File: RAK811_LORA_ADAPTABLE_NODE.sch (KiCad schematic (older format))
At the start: 18 parts, among them J1 Screw_Terminal_01x02, J2 Screw_Terminal_01x03, J3 Conn_01x01_Male, J4 Conn_01x01_Male, J5 Conn_01x01_Male, J6 Conn_01x01_Male, J7 Conn_Coaxial, U1 RAK811-HF

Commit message: some i/o pins layout
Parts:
- removed H1, H6: MountingHole, MountingHole:MountingHole_3mm, symbol Mechanical:MountingHole
- added J10, J11, J12, J13, J14, J15, J8, J9: Conn_01x01_Male, Connector_Wire:SolderWirePad_1x01_Drill0.8mm, symbol Connector:Conn_01x01_Male
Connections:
- net at BT2.2 (-), J7.2 (Ext), U1.1 (GND)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: now also J1.1 (Pin_1), J12.1 (Pin_1); no longer J1.2 (Pin_2)
- net at JP1.2 (C), U1.11 (VCC): now also J1.2 (Pin_2), J15.1 (Pin_1); no longer J1.1 (Pin_1)
- net at U1.13 (PA14): now also J8.1 (Pin_1)
- net at U1.14 (PA15): now also J10.1 (Pin_1)
- net at U1.15 (PB3): now also J13.1 (Pin_1)
- net at U1.16 (PB5): now also J9.1 (Pin_1)
- net at U1.2 (PB12): now also J14.1 (Pin_1)
- net at U1.27 (PB2/BOOT1): now also J11.1 (Pin_1)
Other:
- moved on the sheet: H2, H3, H4, H5
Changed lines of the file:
@@
 $EndDescr
-$Comp
-L Mechanical:MountingHole H1
-U 1 1 5EED2AEB
-P 4200 5600
-F 0 "H1" H 4300 5646 50  0000 L CNN
-F 1 "MountingHole" H 4300 5555 50  0000 L CNN
-F 2 "MountingHole:MountingHole_3mm" H 4200 5600 50  0001 C CNN
-F 3 "~" H 4200 5600 50  0001 C CNN
-	1    4200 5600
-	1    0    0    -1
-$EndComp
 $Comp
 L Mechanical:MountingHole H2
 U 1 1 5EED2E39
-P 4200 5800
-F 0 "H2" H 4300 5846 50  0000 L CNN
-F 1 "MountingHole" H 4300 5755 50  0000 L CNN
-F 2 "MountingHole:MountingHole_3mm" H 4200 5800 50  0001 C CNN
-F 3 "~" H 4200 5800 50  0001 C CNN
-	1    4200 5800
+P 3650 4600
+F 0 "H2" H 3750 4646 50  0000 L CNN
+F 1 "MountingHole" H 3750 4555 50  0000 L CNN
+F 2 "MountingHole:MountingHole_3mm" H 3650 4600 50  0001 C CNN
+F 3 "~" H 3650 4600 50  0001 C CNN
+	1    3650 4600
 	1    0    0    -1
 $EndComp
@@
 L Mechanical:MountingHole H3
 U 1 1 5EED3144
-P 4200 6000
-F 0 "H3" H 4300 6046 50  0000 L CNN
-F 1 "MountingHole" H 4300 5955 50  0000 L CNN
-F 2 "MountingHole:MountingHole_3mm" H 4200 6000 50  0001 C CNN
-F 3 "~" H 4200 6000 50  0001 C CNN
-	1    4200 6000
+P 3650 4800
+F 0 "H3" H 3750 4846 50  0000 L CNN
+F 1 "MountingHole" H 3750 4755 50  0000 L CNN
+F 2 "MountingHole:MountingHole_3mm" H 3650 4800 50  0001 C CNN
+F 3 "~" H 3650 4800 50  0001 C CNN
+	1    3650 4800
 	1    0    0    -1
 $EndComp
@@
 L Mechanical:MountingHole H4
 U 1 1 5EED33AC
-P 5050 5600
-F 0 "H4" H 5150 5646 50  0000 L CNN
-F 1 "MountingHole" H 5150 5555 50  0000 L CNN
-F 2 "MountingHole:MountingHole_3mm" H 5050 5600 50  0001 C CNN
-F 3 "~" H 5050 5600 50  0001 C CNN
-	1    5050 5600
-	1    0    0    -1
-$EndComp
-$Comp
-L Mechanical:MountingHole H6
-U 1 1 5EED36FB
-P 5050 6000
-F 0 "H6" H 5150 6046 50  0000 L CNN
-F 1 "MountingHole" H 5150 5955 50  0000 L CNN
-F 2 "MountingHole:MountingHole_3mm" H 5050 6000 50  0001 C CNN
-F 3 "~" H 5050 6000 50  0001 C CNN
-	1    5050 6000
+P 4500 4400
+F 0 "H4" H 4600 4446 50  0000 L CNN
+F 1 "MountingHole" H 4600 4355 50  0000 L CNN
+F 2 "MountingHole:MountingHole_3mm" H 4500 4400 50  0001 C CNN
+F 3 "~" H 4500 4400 50  0001 C CNN
+	1    4500 4400
 	1    0    0    -1
 $EndComp
@@
 L Mechanical:MountingHole H5
 U 1 1 5EED3A44
-P 5050 5800
-F 0 "H5" H 5150 5846 50  0000 L CNN
-F 1 "MountingHole" H 5150 5755 50  0000 L CNN
-F 2 "MountingHole:MountingHole_3mm" H 5050 5800 50  0001 C CNN
-F 3 "~" H 5050 5800 50  0001 C CNN
-	1    5050 5800
+P 4500 4600
+F 0 "H5" H 4600 4646 50  0000 L CNN
+F 1 "MountingHole" H 4600 4555 50  0000 L CNN
+F 2 "MountingHole:MountingHole_3mm" H 4500 4600 50  0001 C CNN
+F 3 "~" H 4500 4600 50  0001 C CNN
+	1    4500 4600
 	1    0    0    -1
 $EndComp
@@
 $EndComp
 Wire Wire Line
-	7550 1950 7550 1850
-Wire Wire Line
-	7550 1850 5450 1850
-Connection ~ 5450 1850
-Wire Wire Line
-	7550 2050 7000 2050
-Wire Wire Line
-	7000 2050 7000 4200
-Wire Wire Line
 	7000 4200 5850 4200
 Connection ~ 5850 4200
@@
 	7750 4200 7000 4200
 Connection ~ 7000 4200
+Wire Wire Line
+	7550 1950 7000 1950
+Wire Wire Line
+	7000 1950 7000 4200
+Wire Wire Line
+	7550 2050 7150 2050
+Wire Wire Line
+	7150 2050 7150 1850
+Wire Wire Line
+	7150 1850 5450 1850
+Connection ~ 5450 1850
+$Comp
+L Connector:Conn_01x01_Male J8
+U 1 1 5EF586B6
+P 4150 3150
+F 0 "J8" H 4258 3331 50  0000 C CNN
+F 1 "Conn_01x01_Male" H 4258 3240 50  0000 C CNN
+F 2 "Connector_Wire:SolderWirePad_1x01_Drill0.8mm" H 4150 3150 50  0001 C CNN
+F 3 "~" H 4150 3150 50  0001 C CNN
+	1    4150 3150
+	1    0    0    -1
+$EndComp
+Wire Wire Line
+	4350 3150 4550 3150
+$Comp
+L Connector:Conn_01x01_Male J9
+U 1 1 5EF61769
+P 6750 2650
+F 0 "J9" H 6722 2674 50  0000 R CNN
+F 1 "Conn_01x01_Male" H 6722 2583 50  0000 R CNN
+F 2 "Connector_Wire:SolderWirePad_1x01_Drill0.8mm" H 6750 2650 50  0001 C CNN
+F 3 "~" H 6750 2650 50  0001 C CNN
+	1    6750 2650
+	-1   0    0    -1
+$EndComp
+$Comp
+L Connector:Conn_01x01_Male J10
+U 1 1 5EF6CBB4
+P 4150 3250
+F 0 "J10" H 4258 3431 50  0000 C CNN
+F 1 "Conn_01x01_Male" H 4258 3340 50  0000 C CNN
+F 2 "Connector_Wire:SolderWirePad_1x01_Drill0.8mm" H 4150 3250 50  0001 C CNN
+F 3 "~" H 4150 3250 50  0001 C CNN
+	1    4150 3250
+	1    0    0    -1
+$EndComp
+Wire Wire Line
+	4350 3250 4550 3250
+$Comp
+L Connector:Conn_01x01_Male J11
+U 1 1 5EF78D3D
+P 6750 2350
+F 0 "J11" H 6722 2374 50  0000 R CNN
+F 1 "Conn_01x01_Male" H 6722 2283 50  0000 R CNN
+F 2 "Connector_Wire:SolderWirePad_1x01_Drill0.8mm" H 6750 2350 50  0001 C CNN
+F 3 "~" H 6750 2350 50  0001 C CNN
+	1    6750 2350
+	-1   0    0    -1
+$EndComp
+$Comp
+L Connector:Conn_01x01_Male J12
+U 1 1 5EF83DA7
+P 6150 4400
+F 0 "J12" H 6122 4424 50  0000 R CNN
+F 1 "Conn_01x01_Male" H 6122 4333 50  0000 R CNN
+F 2 "Connector_Wire:SolderWirePad_1x01_Drill0.8mm" H 6150 4400 50  0001 C CNN
+F 3 "~" H 6150 4400 50  0001 C CNN
+	1    6150 4400
+	-1   0    0    -1
+$EndComp
+Wire Wire Line
+	5950 4400 5850 4400
+Wire Wire Line
+	5850 4400 5850 4200
+$Comp
+L Connector:Conn_01x01_Male J13
+U 1 1 5EF91077
+P 6750 2450
+F 0 "J13" H 6722 2474 50  0000 R CNN
+F 1 "Conn_01x01_Male" H 6722 2383 50  0000 R CNN
+F 2 "Connector_Wire:SolderWirePad_1x01_Drill0.8mm" H 6750 2450 50  0001 C CNN
+F 3 "~" H 6750 2450 50  0001 C CNN
+	1    6750 2450
+	-1   0    0    -1
+$EndComp
+Wire Wire Line
+	6350 2450 6550 2450
+$Comp
+L Connector:Conn_01x01_Male J14
+U 1 1 5EF9D3AA
+P 6750 3150
+F 0 "J14" H 6722 3174 50  0000 R CNN
+F 1 "Conn_01x01_Male" H 6722 3083 50  0000 R CNN
+F 2 "Connector_Wire:SolderWirePad_1x01_Drill0.8mm" H 6750 3150 50  0001 C CNN
+F 3 "~" H 6750 3150 50  0001 C CNN
+	1    6750 3150
+	-1   0    0    -1
+$EndComp
+Wire Wire Line
+	6350 3150 6550 3150
+$Comp
+L Connector:Conn_01x01_Male J15
+U 1 1 5EFB7B96
+P 5750 1700
+F 0 "J15" H 5722 1724 50  0000 R CNN
+F 1 "Conn_01x01_Male" H 5722 1633 50  0000 R CNN
+F 2 "Connector_Wire:SolderWirePad_1x01_Drill0.8mm" H 5750 1700 50  0001 C CNN
+F 3 "~" H 5750 1700 50  0001 C CNN
+	1    5750 1700
+	-1   0    0    -1
+$EndComp
+Wire Wire Line
+	5550 1700 5450 1700
+Wire Wire Line
+	5450 1700 5450 1850
+Wire Wire Line
+	6350 2350 6550 2350
+Wire Wire Line
+	6350 2650 6550 2650
 $EndSCHEMATC

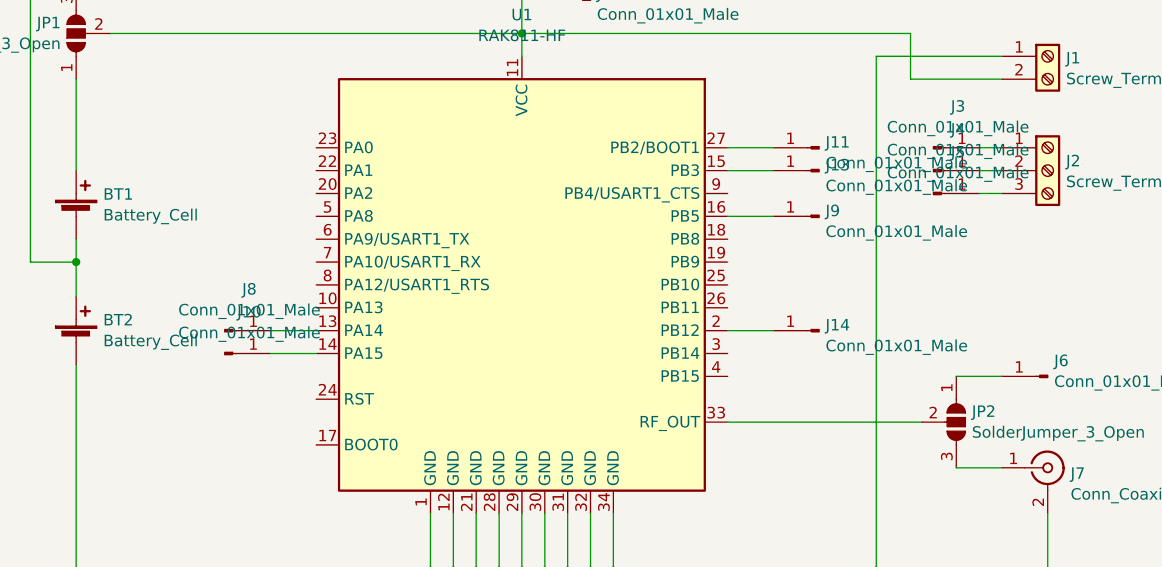
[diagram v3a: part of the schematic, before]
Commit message: half i/o pins layout
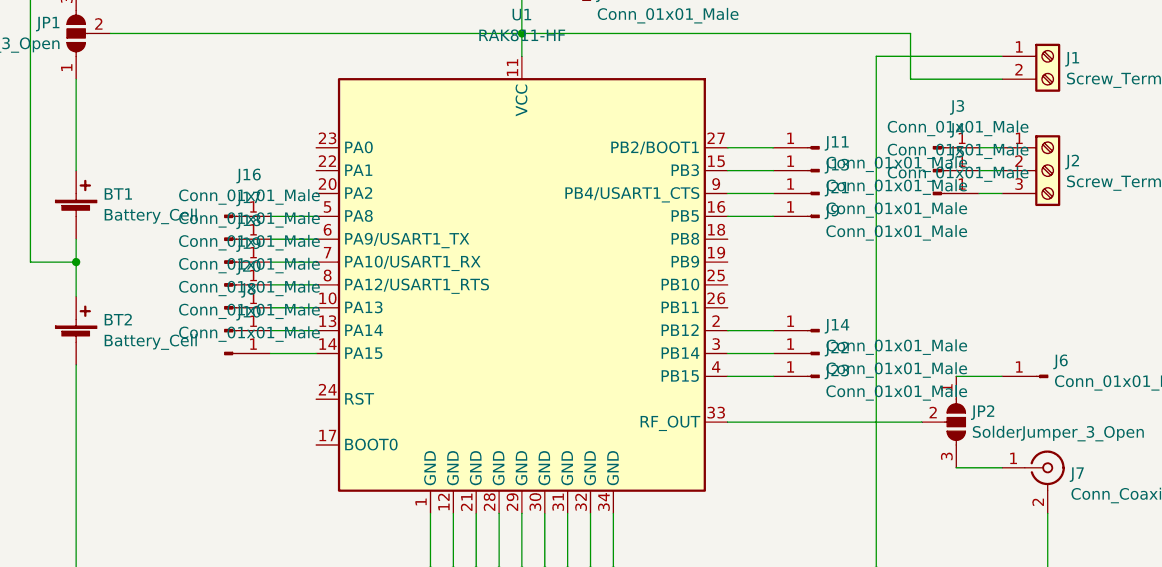
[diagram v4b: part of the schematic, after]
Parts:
- added J16, J17, J18, J19, J20, J21, J22, J23: Conn_01x01_Male, Connector_Wire:SolderWirePad_1x01_Drill0.8mm, symbol Connector:Conn_01x01_Male
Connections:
- net at U1.10 (PA13): now also J20.1 (Pin_1)
- net at U1.3 (PB14): now also J22.1 (Pin_1)
- net at U1.4 (PB15): now also J23.1 (Pin_1)
- net at U1.5 (PA8): now also J16.1 (Pin_1)
- net at U1.6 (PA9/USART1_TX): now also J17.1 (Pin_1)
- net at U1.7 (PA10/USART1_RX): now also J18.1 (Pin_1)
- net at U1.8 (PA12/USART1_RTS): now also J19.1 (Pin_1)
- net at U1.9 (PB4/USART1_CTS): now also J21.1 (Pin_1)
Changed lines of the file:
@@
 Wire Wire Line
 	6350 2650 6550 2650
+$Comp
+L Connector:Conn_01x01_Male J22
+U 1 1 5EFEF2F6
+P 6750 3250
+F 0 "J22" H 6722 3274 50  0000 R CNN
+F 1 "Conn_01x01_Male" H 6722 3183 50  0000 R CNN
+F 2 "Connector_Wire:SolderWirePad_1x01_Drill0.8mm" H 6750 3250 50  0001 C CNN
+F 3 "~" H 6750 3250 50  0001 C CNN
+	1    6750 3250
+	-1   0    0    -1
+$EndComp
+$Comp
+L Connector:Conn_01x01_Male J23
+U 1 1 5EFEFE07
+P 6750 3350
+F 0 "J23" H 6722 3374 50  0000 R CNN
+F 1 "Conn_01x01_Male" H 6722 3283 50  0000 R CNN
+F 2 "Connector_Wire:SolderWirePad_1x01_Drill0.8mm" H 6750 3350 50  0001 C CNN
+F 3 "~" H 6750 3350 50  0001 C CNN
+	1    6750 3350
+	-1   0    0    -1
+$EndComp
+$Comp
+L Connector:Conn_01x01_Male J16
+U 1 1 5EFF0C86
+P 4150 2650
+F 0 "J16" H 4258 2831 50  0000 C CNN
+F 1 "Conn_01x01_Male" H 4258 2740 50  0000 C CNN
+F 2 "Connector_Wire:SolderWirePad_1x01_Drill0.8mm" H 4150 2650 50  0001 C CNN
+F 3 "~" H 4150 2650 50  0001 C CNN
+	1    4150 2650
+	1    0    0    -1
+$EndComp
+$Comp
+L Connector:Conn_01x01_Male J17
+U 1 1 5EFF1821
+P 4150 2750
+F 0 "J17" H 4258 2931 50  0000 C CNN
+F 1 "Conn_01x01_Male" H 4258 2840 50  0000 C CNN
+F 2 "Connector_Wire:SolderWirePad_1x01_Drill0.8mm" H 4150 2750 50  0001 C CNN
+F 3 "~" H 4150 2750 50  0001 C CNN
+	1    4150 2750
+	1    0    0    -1
+$EndComp
+$Comp
+L Connector:Conn_01x01_Male J18
+U 1 1 5EFF2375
+P 4150 2850
+F 0 "J18" H 4258 3031 50  0000 C CNN
+F 1 "Conn_01x01_Male" H 4258 2940 50  0000 C CNN
+F 2 "Connector_Wire:SolderWirePad_1x01_Drill0.8mm" H 4150 2850 50  0001 C CNN
+F 3 "~" H 4150 2850 50  0001 C CNN
+	1    4150 2850
+	1    0    0    -1
+$EndComp
+$Comp
+L Connector:Conn_01x01_Male J19
+U 1 1 5EFF2EEE
+P 4150 2950
+F 0 "J19" H 4258 3131 50  0000 C CNN
+F 1 "Conn_01x01_Male" H 4258 3040 50  0000 C CNN
+F 2 "Connector_Wire:SolderWirePad_1x01_Drill0.8mm" H 4150 2950 50  0001 C CNN
+F 3 "~" H 4150 2950 50  0001 C CNN
+	1    4150 2950
+	1    0    0    -1
+$EndComp
+$Comp
+L Connector:Conn_01x01_Male J21
+U 1 1 5EFF38A2
+P 6750 2550
+F 0 "J21" H 6722 2574 50  0000 R CNN
+F 1 "Conn_01x01_Male" H 6722 2483 50  0000 R CNN
+F 2 "Connector_Wire:SolderWirePad_1x01_Drill0.8mm" H 6750 2550 50  0001 C CNN
+F 3 "~" H 6750 2550 50  0001 C CNN
+	1    6750 2550
+	-1   0    0    -1
+$EndComp
+$Comp
+L Connector:Conn_01x01_Male J20
+U 1 1 5EFF3ECF
+P 4150 3050
+F 0 "J20" H 4258 3231 50  0000 C CNN
+F 1 "Conn_01x01_Male" H 4258 3140 50  0000 C CNN
+F 2 "Connector_Wire:SolderWirePad_1x01_Drill0.8mm" H 4150 3050 50  0001 C CNN
+F 3 "~" H 4150 3050 50  0001 C CNN
+	1    4150 3050
+	1    0    0    -1
+$EndComp
+Wire Wire Line
+	6350 3250 6550 3250
+Wire Wire Line
+	6350 3350 6550 3350
+Wire Wire Line
+	4350 2650 4550 2650
+Wire Wire Line
+	4350 2750 4550 2750
+Wire Wire Line
+	4350 2850 4550 2850
+Wire Wire Line
+	4350 2950 4550 2950
+Wire Wire Line
+	6350 2550 6550 2550
+Wire Wire Line
+	4350 3050 4550 3050
 $EndSCHEMATC

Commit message: all i/o pins layout
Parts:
- added J24, J25, J26, J27, J28, J29, J30, J31, J32: Conn_01x01_Male, Connector_Wire:SolderWirePad_1x01_Drill0.8mm, symbol Connector:Conn_01x01_Male
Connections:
- net at U1.17 (BOOT0): now also J28.1 (Pin_1)
- net at U1.18 (PB8): now also J29.1 (Pin_1)
- net at U1.19 (PB9): now also J30.1 (Pin_1)
- net at U1.20 (PA2): now also J26.1 (Pin_1)
- net at U1.22 (PA1): now also J25.1 (Pin_1)
- net at U1.23 (PA0): now also J24.1 (Pin_1)
- net at U1.24 (RST): now also J27.1 (Pin_1)
- net at U1.25 (PB10): now also J31.1 (Pin_1)
- net at U1.26 (PB11): now also J32.1 (Pin_1)
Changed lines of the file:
@@
 Wire Wire Line
 	4350 3050 4550 3050
+$Comp
+L Connector:Conn_01x01_Male J26
+U 1 1 5EF46CC4
+P 4150 2550
+F 0 "J26" H 4258 2731 50  0000 C CNN
+F 1 "Conn_01x01_Male" H 4258 2640 50  0000 C CNN
+F 2 "Connector_Wire:SolderWirePad_1x01_Drill0.8mm" H 4150 2550 50  0001 C CNN
+F 3 "~" H 4150 2550 50  0001 C CNN
+	1    4150 2550
+	1    0    0    -1
+$EndComp
+$Comp
+L Connector:Conn_01x01_Male J25
+U 1 1 5EF4A3F0
+P 4150 2450
+F 0 "J25" H 4258 2631 50  0000 C CNN
+F 1 "Conn_01x01_Male" H 4258 2540 50  0000 C CNN
+F 2 "Connector_Wire:SolderWirePad_1x01_Drill0.8mm" H 4150 2450 50  0001 C CNN
+F 3 "~" H 4150 2450 50  0001 C CNN
+	1    4150 2450
+	1    0    0    -1
+$EndComp
+$Comp
+L Connector:Conn_01x01_Male J24
+U 1 1 5EF4DB52
+P 4150 2350
+F 0 "J24" H 4258 2531 50  0000 C CNN
+F 1 "Conn_01x01_Male" H 4258 2440 50  0000 C CNN
+F 2 "Connector_Wire:SolderWirePad_1x01_Drill0.8mm" H 4150 2350 50  0001 C CNN
+F 3 "~" H 4150 2350 50  0001 C CNN
+	1    4150 2350
+	1    0    0    -1
+$EndComp
+$Comp
+L Connector:Conn_01x01_Male J27
+U 1 1 5EF4EB2E
+P 4150 3450
+F 0 "J27" H 4258 3631 50  0000 C CNN
+F 1 "Conn_01x01_Male" H 4258 3540 50  0000 C CNN
+F 2 "Connector_Wire:SolderWirePad_1x01_Drill0.8mm" H 4150 3450 50  0001 C CNN
+F 3 "~" H 4150 3450 50  0001 C CNN
+	1    4150 3450
+	1    0    0    -1
+$EndComp
+$Comp
+L Connector:Conn_01x01_Male J28
+U 1 1 5EF4F1F7
+P 4150 3650
+F 0 "J28" H 4258 3831 50  0000 C CNN
+F 1 "Conn_01x01_Male" H 4258 3740 50  0000 C CNN
+F 2 "Connector_Wire:SolderWirePad_1x01_Drill0.8mm" H 4150 3650 50  0001 C CNN
+F 3 "~" H 4150 3650 50  0001 C CNN
+	1    4150 3650
+	1    0    0    -1
+$EndComp
+$Comp
+L Connector:Conn_01x01_Male J29
+U 1 1 5EF50306
+P 6750 2750
+F 0 "J29" H 6722 2774 50  0000 R CNN
+F 1 "Conn_01x01_Male" H 6722 2683 50  0000 R CNN
+F 2 "Connector_Wire:SolderWirePad_1x01_Drill0.8mm" H 6750 2750 50  0001 C CNN
+F 3 "~" H 6750 2750 50  0001 C CNN
+	1    6750 2750
+	-1   0    0    -1
+$EndComp
+$Comp
+L Connector:Conn_01x01_Male J30
+U 1 1 5EF5185E
+P 6750 2850
+F 0 "J30" H 6722 2874 50  0000 R CNN
+F 1 "Conn_01x01_Male" H 6722 2783 50  0000 R CNN
+F 2 "Connector_Wire:SolderWirePad_1x01_Drill0.8mm" H 6750 2850 50  0001 C CNN
+F 3 "~" H 6750 2850 50  0001 C CNN
+	1    6750 2850
+	-1   0    0    -1
+$EndComp
+$Comp
+L Connector:Conn_01x01_Male J31
+U 1 1 5EF52224
+P 6750 2950
+F 0 "J31" H 6722 2974 50  0000 R CNN
+F 1 "Conn_01x01_Male" H 6722 2883 50  0000 R CNN
+F 2 "Connector_Wire:SolderWirePad_1x01_Drill0.8mm" H 6750 2950 50  0001 C CNN
+F 3 "~" H 6750 2950 50  0001 C CNN
+	1    6750 2950
+	-1   0    0    -1
+$EndComp
+$Comp
+L Connector:Conn_01x01_Male J32
+U 1 1 5EF527FE
+P 6750 3050
+F 0 "J32" H 6722 3074 50  0000 R CNN
+F 1 "Conn_01x01_Male" H 6722 2983 50  0000 R CNN
+F 2 "Connector_Wire:SolderWirePad_1x01_Drill0.8mm" H 6750 3050 50  0001 C CNN
+F 3 "~" H 6750 3050 50  0001 C CNN
+	1    6750 3050
+	-1   0    0    -1
+$EndComp
+Wire Wire Line
+	4350 2550 4550 2550
+Wire Wire Line
+	4350 2450 4550 2450
+Wire Wire Line
+	4350 2350 4550 2350
+Wire Wire Line
+	4350 3450 4550 3450
+Wire Wire Line
+	4350 3650 4550 3650
+Wire Wire Line
+	6350 2750 6550 2750
+Wire Wire Line
+	6350 2850 6550 2850
+Wire Wire Line
+	6350 2950 6550 2950
+Wire Wire Line
+	6350 3050 6550 3050
 $EndSCHEMATC
